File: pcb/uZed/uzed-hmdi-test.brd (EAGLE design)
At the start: 86.4 x 56.5 mm, 20 parts, among them J5 HDMI-TYPE-A-RECEPTICALFCI1002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, J6 HDMI-TYPE-A-RECEPTICALFCI1002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

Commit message: more work on hdmi -test
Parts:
- moved U$1 20.0 mm to (14.9, 29.0), turned to 180 degrees
- moved R5 10.3 mm to (11.2, 23.0)
- moved RN7 2.45 mm to (18.0, 26.4)
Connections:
- net N$11 renamed HDMI_PU
- new net N$13: JX2.P$65
- new net N$17: JX2.P$63
- new net N$6: JX2.P$77
- new net N$7: JX2.P$75
- new net N$8: JX2.P$71
- new net N$9: JX2.P$69
- net P2_CLOCK+: now also JX2.P$83
- net P2_CLOCK-: now also JX2.P$81
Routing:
- net P2_CLOCK-: track 0.00 -> 43.6 mm
- net HDMI_PU: track 0.00 -> 4.03 mm, vias 0 -> 2
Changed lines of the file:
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@@
 <?xml version="1.0" encoding="utf-8"?>
 <!DOCTYPE eagle SYSTEM "eagle.dtd">
-<eagle version="8.6.1">
+<eagle version="8.7.0">
 <drawing>
 <settings>
@@
 <dimension x1="14.605" y1="49.53" x2="10.795" y2="49.53" x3="12.7" y3="66.04" textsize="1.778" layer="1" dtype="diameter" unit="inch"/>
 <dimension x1="10.795" y1="50.165" x2="61.595" y2="50.165" x3="36.195" y3="72.39" textsize="1.778" layer="1" dtype="diameter" unit="mil"/>
-<dimension x1="38.1" y1="50.8" x2="82.55" y2="50.8" x3="60.325" y3="60.96" textsize="1.778" layer="1" dtype="diameter" unit="mil"/>
 <dimension x1="39.37" y1="50.8" x2="61.595" y2="50.8" x3="50.4825" y3="67.31" textsize="1.778" layer="1" dtype="diameter" unit="mil"/>
 </plain>
@@
 </element>
 <element name="R4" library="rcl" package="R0603" value="10K" x="14.224" y="43.942"/>
-<element name="R5" library="rcl" package="R0603" value="10K" x="16.51" y="31.75"/>
+<element name="R5" library="rcl" package="R0603" value="10K" x="11.176" y="22.987"/>
 <element name="R6" library="rcl" package="R0603" value="10K" x="14.351" y="46.355"/>
 <element name="R7" library="rcl" package="R0603" value="0" x="26.67" y="22.733"/>
@@
 <attribute name="OC_NEWARK" value="unknown" x="14.732" y="10.033" size="1.778" layer="27" rot="R270" display="off"/>
 </element>
-<element name="RN7" library="resistor-dil" package="0603-ARV" value="2k" x="20.32" y="27.305" rot="R180">
-<attribute name="MF" value="" x="20.32" y="27.305" size="1.778" layer="27" rot="R180" display="off"/>
-<attribute name="MPN" value="" x="20.32" y="27.305" size="1.778" layer="27" rot="R180" display="off"/>
-<attribute name="OC_FARNELL" value="unknown" x="20.32" y="27.305" size="1.778" layer="27" rot="R180" display="off"/>
-<attribute name="OC_NEWARK" value="unknown" x="20.32" y="27.305" size="1.778" layer="27" rot="R180" display="off"/>
+<element name="RN7" library="resistor-dil" package="0603-ARV" value="2k" x="18.034" y="26.416" rot="R180">
+<attribute name="MF" value="" x="18.034" y="26.416" size="1.778" layer="27" rot="R180" display="off"/>
+<attribute name="MPN" value="" x="18.034" y="26.416" size="1.778" layer="27" rot="R180" display="off"/>
+<attribute name="OC_FARNELL" value="unknown" x="18.034" y="26.416" size="1.778" layer="27" rot="R180" display="off"/>
+<attribute name="OC_NEWARK" value="unknown" x="18.034" y="26.416" size="1.778" layer="27" rot="R180" display="off"/>
 </element>
-<element name="U$1" library="lupa300-components" package="SOT23" value="BSS138" x="19.05" y="48.514"/>
+<element name="U$1" library="lupa300-components" package="SOT23" value="BSS138" x="14.859" y="28.956" rot="R180"/>
 </elements>
 <signals>
@@
 <wire x1="31.076" y1="20.447" x2="72.48" y2="8.575" width="0" layer="19" extent="1-1"/>
 <wire x1="21.459" y1="22.757" x2="31.076" y2="20.447" width="0" layer="19" extent="1-1"/>
-<wire x1="21.52" y1="27.93" x2="21.459" y2="22.757" width="0" layer="19" extent="1-1"/>
-<wire x1="20.72" y1="27.93" x2="21.52" y2="27.93" width="0" layer="19" extent="1-1"/>
-<wire x1="13.501" y1="46.355" x2="21.52" y2="27.93" width="0" layer="19" extent="1-1"/>
+<wire x1="19.234" y1="27.041" x2="21.459" y2="22.757" width="0" layer="19" extent="1-1"/>
+<wire x1="18.434" y1="27.041" x2="19.234" y2="27.041" width="0" layer="19" extent="1-1"/>
+<wire x1="13.501" y1="46.355" x2="18.434" y2="27.041" width="0" layer="19" extent="1-1"/>
 </signal>
 <signal name="GND">
@@
 <wire x1="64.48" y1="8.575" x2="64.48" y2="48.625" width="0" layer="19" extent="1-1"/>
 <wire x1="25.82" y1="22.733" x2="64.48" y2="8.575" width="0" layer="19" extent="1-1"/>
-<wire x1="19.12" y1="27.93" x2="25.82" y2="22.733" width="0" layer="19" extent="1-1"/>
-<wire x1="19.92" y1="27.93" x2="19.12" y2="27.93" width="0" layer="19" extent="1-1"/>
-<wire x1="18.409" y1="22.757" x2="19.92" y2="27.93" width="0" layer="19" extent="1-1"/>
+<wire x1="18.409" y1="22.757" x2="25.82" y2="22.733" width="0" layer="19" extent="1-1"/>
 <wire x1="18.409" y1="22.257" x2="18.409" y2="22.757" width="0" layer="19" extent="1-1"/>
-<wire x1="17.36" y1="31.75" x2="19.92" y2="27.93" width="0" layer="19" extent="1-1"/>
-<wire x1="8.57" y1="20.51" x2="18.409" y2="22.257" width="0" layer="19" extent="1-1"/>
+<wire x1="17.634" y1="27.041" x2="18.409" y2="22.757" width="0" layer="19" extent="1-1"/>
+<wire x1="16.834" y1="27.041" x2="17.634" y2="27.041" width="0" layer="19" extent="1-1"/>
+<wire x1="12.026" y1="22.987" x2="16.834" y2="27.041" width="0" layer="19" extent="1-1"/>
+<wire x1="8.57" y1="20.51" x2="12.026" y2="22.987" width="0" layer="19" extent="1-1"/>
 </signal>
 <signal name="VCCIO_EN">
@@
 <wire x1="21.209" y1="17.653" x2="49.784" y2="17.653" width="0.3048" layer="1"/>
 </signal>
-<signal name="N$11">
+<signal name="HDMI_PU">
 <contactref element="RN4" pad="3"/>
 <contactref element="RN4" pad="4"/>
@@
 <contactref element="RN3" pad="3"/>
 <contactref element="RN6" pad="3"/>
-<wire x1="15.305" y1="19.423" x2="29.376" y2="20.447" width="0" layer="19" extent="1-1"/>
-<wire x1="15.305" y1="18.423" x2="15.305" y2="19.423" width="0" layer="19" extent="1-1"/>
+<wire x1="15.305" y1="19.423" x2="15.305" y2="18.923" width="0.508" layer="1"/>
+<wire x1="15.305" y1="18.923" x2="15.305" y2="18.423" width="0.508" layer="1"/>
+<wire x1="15.305" y1="18.923" x2="16.383" y2="18.923" width="0.508" layer="1"/>
+<via x="16.383" y="18.923" extent="1-16" drill="0.4" diameter="0.8"/>
+<wire x1="15.305" y1="16.502" x2="15.305" y2="16.002" width="0.508" layer="1"/>
+<wire x1="15.305" y1="16.002" x2="15.305" y2="15.502" width="0.508" layer="1"/>
+<wire x1="15.305" y1="16.002" x2="16.256" y2="16.002" width="0.508" layer="1"/>
+<via x="16.256" y="16.002" extent="1-16" drill="0.4" diameter="0.8"/>
+<wire x1="16.383" y1="18.923" x2="29.376" y2="20.447" width="0" layer="19" extent="1-1"/>
 <wire x1="15.305" y1="16.502" x2="15.305" y2="18.423" width="0" layer="19" extent="1-1"/>
-<wire x1="15.305" y1="15.502" x2="15.305" y2="16.502" width="0" layer="19" extent="1-1"/>
 <wire x1="15.305" y1="13.454" x2="15.305" y2="15.502" width="0" layer="19" extent="1-1"/>
 <wire x1="15.305" y1="12.454" x2="15.305" y2="13.454" width="0" layer="19" extent="1-1"/>
@@
 <contactref element="R5" pad="1"/>
 <contactref element="U$1" pad="3"/>
-<wire x1="15.66" y1="31.75" x2="19.05" y2="49.614" width="0" layer="19" extent="1-1"/>
-<wire x1="8.57" y1="21.01" x2="15.66" y2="31.75" width="0" layer="19" extent="1-1"/>
+<wire x1="10.326" y1="22.987" x2="14.859" y2="27.856" width="0" layer="19" extent="1-1"/>
+<wire x1="8.57" y1="21.01" x2="10.326" y2="22.987" width="0" layer="19" extent="1-1"/>
 </signal>
 <signal name="N$15">
@@
 <wire x1="15.375" y1="23.757" x2="18.409" y2="23.757" width="0.3048" layer="1"/>
 <wire x1="11.128" y1="19.51" x2="15.375" y2="23.757" width="0.3048" layer="1"/>
-<wire x1="18.409" y1="23.757" x2="19.12" y2="26.68" width="0" layer="19" extent="1-1"/>
+<wire x1="15.375" y1="23.757" x2="16.834" y2="25.791" width="0" layer="19" extent="1-1"/>
 </signal>
 <signal name="N$16">
@@
 <wire x1="15.52158125" y1="23.257" x2="18.409" y2="23.257" width="0.3048" layer="1"/>
 <wire x1="8.6128" y1="19.0528" x2="11.31738125" y2="19.0528" width="0.3048" layer="1"/>
-<wire x1="18.409" y1="23.257" x2="19.92" y2="26.68" width="0" layer="19" extent="1-1"/>
+<wire x1="18.409" y1="23.257" x2="17.634" y2="25.791" width="0" layer="19" extent="1-1"/>
 </signal>
 <signal name="SCL2">
 <contactref element="PCA9306" pad="3"/>
 <contactref element="RN7" pad="8"/>
-<wire x1="21.459" y1="23.257" x2="21.52" y2="26.68" width="0" layer="19" extent="1-1"/>
+<wire x1="19.234" y1="25.791" x2="21.459" y2="23.257" width="0" layer="19" extent="1-1"/>
 </signal>
 <signal name="SDA2">
 <contactref element="PCA9306" pad="4"/>
 <contactref element="RN7" pad="7"/>
-<wire x1="21.459" y1="23.757" x2="20.72" y2="26.68" width="0" layer="19" extent="1-1"/>
+<wire x1="18.434" y1="25.791" x2="21.459" y2="23.757" width="0" layer="19" extent="1-1"/>
 </signal>
 <signal name="P2_DATA2+">
@@
 <signal name="P2_CLOCK+">
 <contactref element="J5" pad="10"/>
+<contactref element="JX2" pad="P$83"/>
+<wire x1="8.57" y1="38.735" x2="48.48" y2="48.625" width="0" layer="19" extent="1-1"/>
 </signal>
 <signal name="P2_CLOCK-">
 <contactref element="J5" pad="12"/>
+<contactref element="JX2" pad="P$81"/>
+<wire x1="8.57" y1="39.735" x2="42.783" y2="39.735" width="0.1524" layer="1"/>
+<wire x1="42.783" y1="39.735" x2="49.403" y2="46.355" width="0.1524" layer="1"/>
+<wire x1="49.403" y1="46.355" x2="49.28" y2="48.625" width="0" layer="19" extent="1-1"/>
 </signal>
 <signal name="DET_CONTROL">
 <contactref element="U$1" pad="1"/>
 <contactref element="R6" pad="2"/>
-<wire x1="15.201" y1="46.355" x2="18.1" y2="47.414" width="0" layer="19" extent="1-1"/>
+<wire x1="15.809" y1="30.056" x2="15.201" y2="46.355" width="0" layer="19" extent="1-1"/>
 </signal>
 <signal name="N$14">
@@
 <contactref element="JX2" pad="P$12"/>
 </signal>
+<signal name="N$6">
+<contactref element="JX2" pad="P$77"/>
+</signal>
+<signal name="N$7">
+<contactref element="JX2" pad="P$75"/>
+</signal>
+<signal name="N$8">
+<contactref element="JX2" pad="P$71"/>
+</signal>
+<signal name="N$9">
+<contactref element="JX2" pad="P$69"/>
+</signal>
+<signal name="N$13">
+<contactref element="JX2" pad="P$65"/>
+</signal>
+<signal name="N$17">
+<contactref element="JX2" pad="P$63"/>
+</signal>
 </signals>

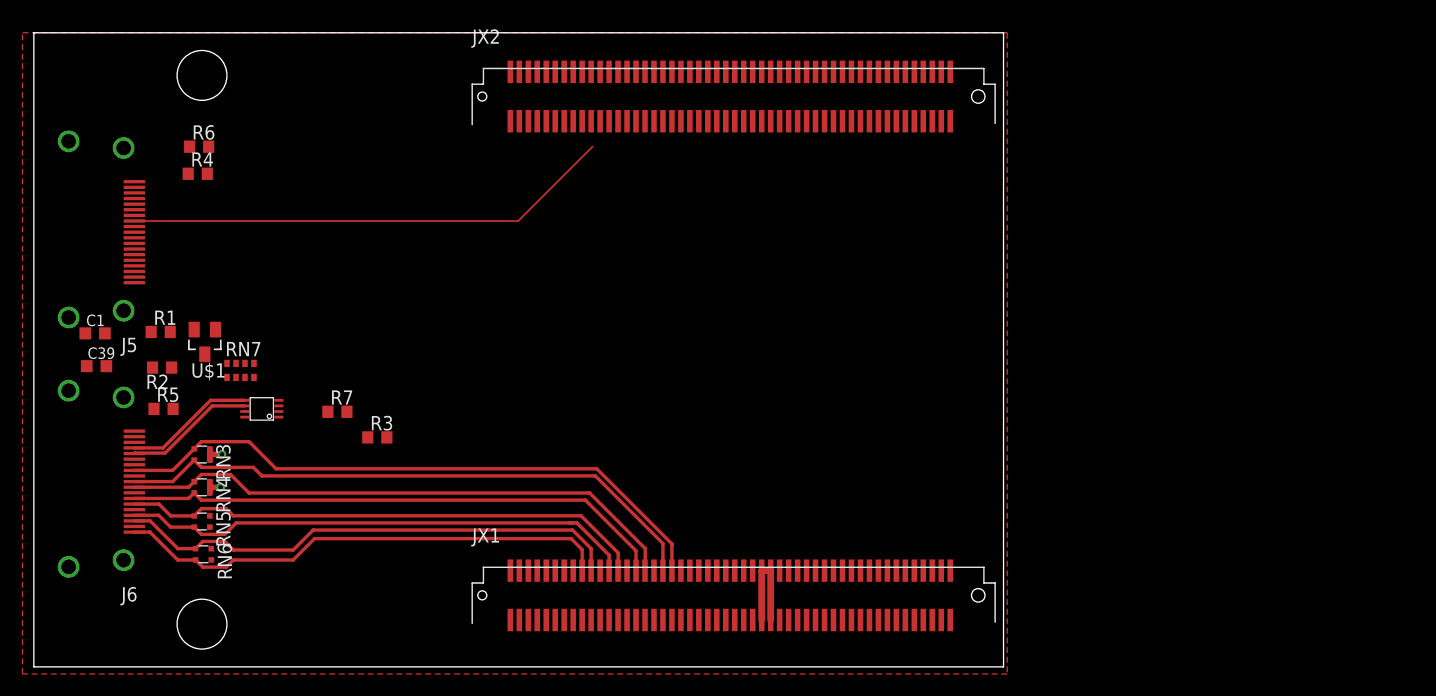
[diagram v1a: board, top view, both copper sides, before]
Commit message: full sized hdmi test
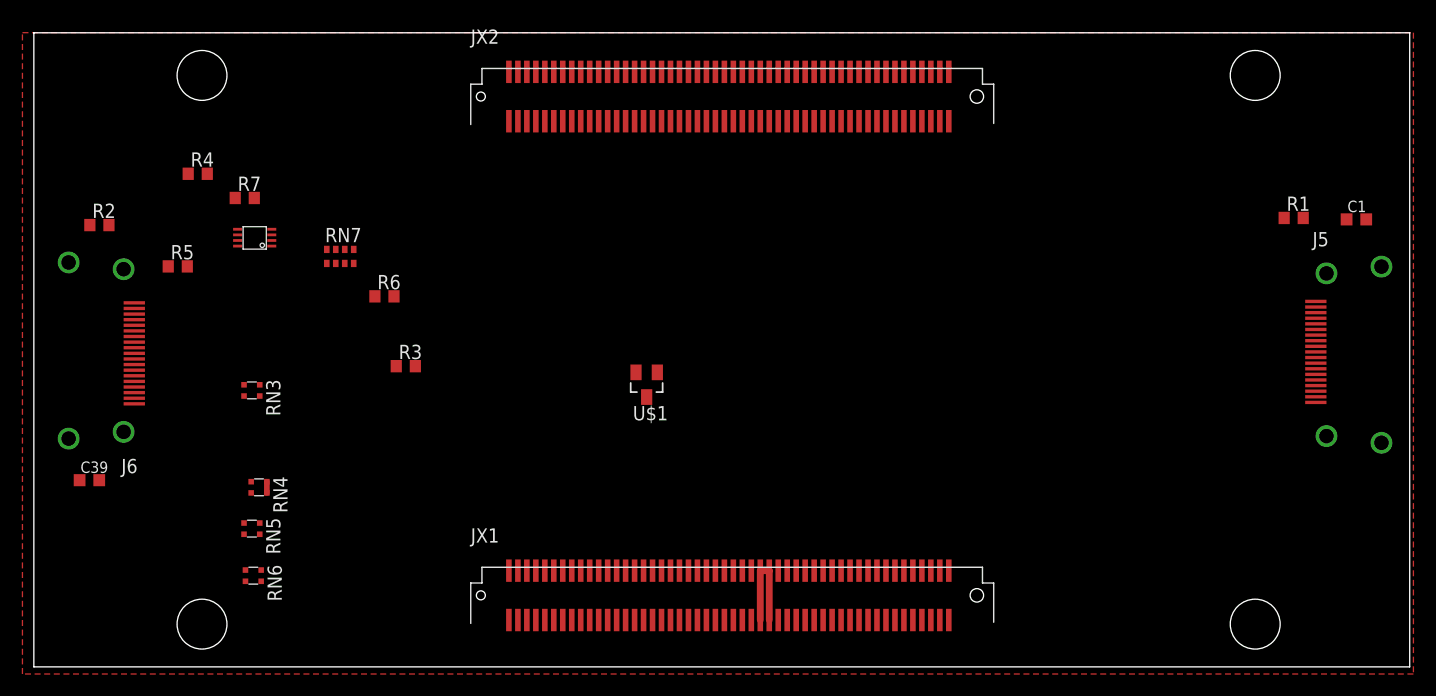
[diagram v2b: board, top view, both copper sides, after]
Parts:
- moved C1 112.9 mm to (117.5, 39.9)
- moved J5 107.7 mm to (114.8, 28.1), turned to 0 degrees
- moved R1 101.5 mm to (111.9, 40.0)
- moved U$1 39.6 mm to (54.2, 25.1)
- moved R6 21.2 mm to (30.9, 33.0)
- moved R7 20.8 mm to (18.4, 41.8)
- moved PCA9306 15.3 mm to (19.3, 38.2)
- moved R2 13.9 mm to (5.46, 39.4), turned to 0 degrees
- moved RN7 13.5 mm to (26.9, 36.6)
- moved R5 12.8 mm to (12.4, 35.7)
- moved J6 11.4 mm to (7.62, 27.9)
- moved C39 10.2 mm to (4.57, 16.6)
- moved RN3 7.24 mm to (19.1, 24.6)
- moved R3 6.84 mm to (32.8, 26.8)
- moved RN4 5.08 mm to (19.7, 16.0)
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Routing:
- net P1_CLOCK-: track 55.2 -> 0.00 mm
- net P1_CLOCK+: track 53.4 -> 0.00 mm
- net P1_DATA0-: track 50.7 -> 0.00 mm
- net P1_DATA0+: track 48.8 -> 0.00 mm
- net P1_DATA1-: track 47.0 -> 0.00 mm
- net P1_DATA1+: track 46.0 -> 0.00 mm
- net P1_DATA2-: track 45.7 -> 0.00 mm
- net P1_DATA2+: track 44.5 -> 0.00 mm
- net P2_CLOCK-: track 43.6 -> 0.00 mm
- net N$16: track 11.6 -> 0.00 mm
- net N$15: track 11.6 -> 0.00 mm
- net HDMI_PU: track 4.03 -> 1.00 mm, vias 2 -> 0
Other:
- board size 86.4 x 56.5 mm -> 122.6 x 56.5 mm

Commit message: finished hdmi test board
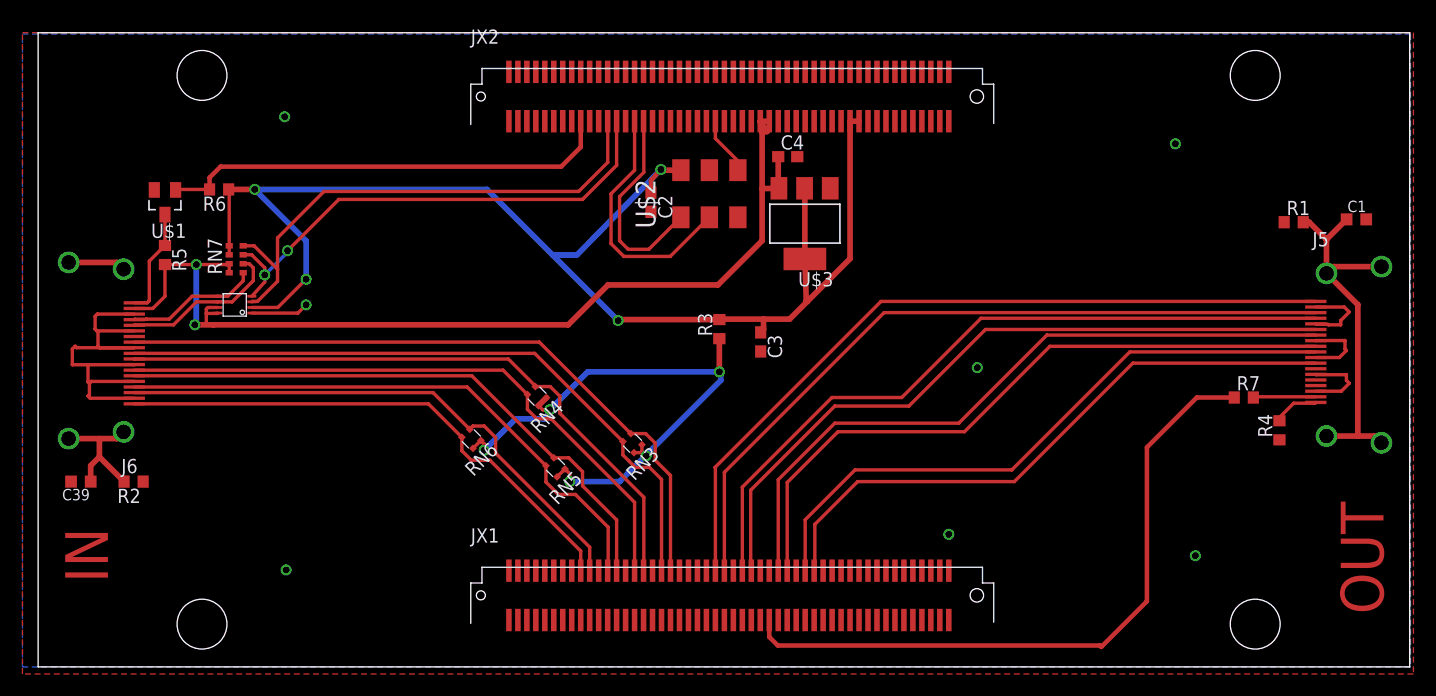
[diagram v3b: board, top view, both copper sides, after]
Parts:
- added C2, C3, C4: (no value), rcl:C0603
- added U$2: SI514, lupa300-components:XTAL-6PIN
- added U$3: SPX1117, lupa300-components:SOT223
- moved R4 99.1 mm to (110.6, 21.1), turned to 90 degrees
- moved R7 90.8 mm to (107.4, 24.0)
- moved U$1 45.9 mm to (11.3, 41.4)
- moved RN3 34.2 mm to (53.0, 19.9), turned to 225 degrees
- moved R3 28.1 mm to (60.7, 30.1), turned to 90 degrees
- moved RN5 27.6 mm to (46.1, 17.8), turned to 225 degrees
- moved RN4 26.1 mm to (44.5, 24.1), turned to 225 degrees
- moved R2 23.1 mm to (8.51, 16.5), turned to 180 degrees
- moved RN6 22.9 mm to (38.6, 20.3), turned to 225 degrees
- moved R6 17.5 mm to (16.1, 42.5), turned to 180 degrees
- moved RN7 9.27 mm to (17.7, 36.3), turned to 270 degrees
- moved PCA9306 6.23 mm to (17.5, 32.3)
- moved R5 1.53 mm to (11.3, 36.7), turned to 270 degrees
- moved C39 0.77 mm to (3.81, 16.5), turned to 180 degrees
- moved R1 0.38 mm to (111.9, 39.6)
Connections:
- removed net N$13: JX2.P$65
- removed net N$17: JX2.P$63
- removed net N$6: JX2.P$77
- removed net N$7: JX2.P$75
- removed net N$8: JX2.P$71
- removed net N$9: JX2.P$69
- new net SCLC: JX2.P$71, U$2.P$2
- new net SDAC: JX2.P$69, U$2.P$1
- net 3V3: now also C2.1, C3.1, U$2.P$6, U$3.2, U$3.4
- net 5V: now also C4.1, U$3.3
- net DET_CONTROL: now also JX2.P$83
- net GND: now also C2.2, C3.2, C4.2, U$2.P$3, U$3.1
- net HDMI_CLOCK: now also JX2.P$53, U$2.P$4; no longer JX1.P$60
- net P2_CLOCK+: now also JX1.P$34; no longer JX2.P$83
- net P2_CLOCK-: now also JX1.P$32; no longer JX2.P$81
- net P2_DATA0+: now also JX1.P$40
- net P2_DATA0-: now also JX1.P$38
- net P2_DATA1+: now also JX1.P$48
- net P2_DATA1-: now also JX1.P$46
- net P2_DATA2+: now also JX1.P$54
- net P2_DATA2-: now also JX1.P$52
- net SCL2: now also JX2.P$77
- net SDA2: now also JX2.P$75
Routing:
- net 5V: track 9.60 -> 152.8 mm, vias 0 -> 2
- net 3V3: track 0.00 -> 125.9 mm, vias 0 -> 4
- net P2_DATA2+: track 0.00 -> 68.9 mm
- net P2_DATA2-: track 0.00 -> 67.4 mm
- net P2_DATA1+: track 0.00 -> 64.8 mm
- net P2_DATA1-: track 0.00 -> 63.5 mm
- net GND: track 0.00 -> 62.2 mm, vias 0 -> 7
- net P1_CLOCK-: track 0.00 -> 62.1 mm
- net P2_DATA0+: track 0.00 -> 61.3 mm
- net P1_CLOCK+: track 0.00 -> 60.5 mm
- net P2_DATA0-: track 0.00 -> 60.0 mm
- net P1_DATA0-: track 0.00 -> 58.0 mm
- net P1_DATA0+: track 0.00 -> 56.3 mm
- net P2_CLOCK+: track 0.00 -> 56.2 mm
- net P2_CLOCK-: track 0.00 -> 54.7 mm
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- added copper zone on layer 16, net GND
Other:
- board size 122.6 x 56.5 mm -> 122.2 x 56.5 mm
- board text added: "IN"
- board text added: "OUT"
